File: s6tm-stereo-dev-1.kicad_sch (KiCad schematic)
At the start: 40 parts, among them J10 Conn_01x04_Pin, J3 USB_C_Receptacle_USB2.0_14P, SW1 SW_SPDT, SW10 SW_Push, SW5 SW_Push, SW6 SW_Push, SW7 SW_Push, SW9 SW_Push, U4 ESP32-S3FN8, Y1 48M

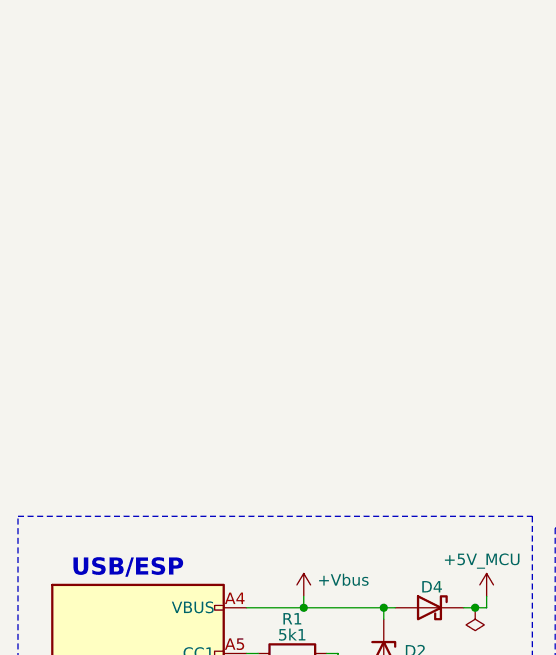
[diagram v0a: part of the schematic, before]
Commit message: schem: add led pwr status
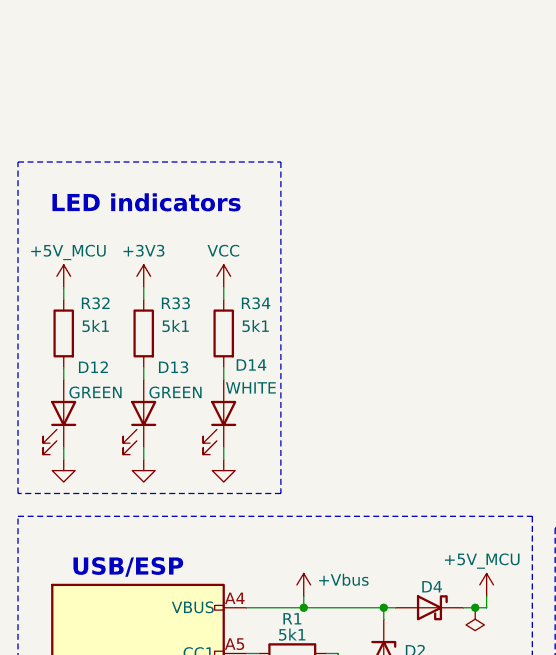
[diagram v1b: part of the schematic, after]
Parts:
- added D12, D13: GREEN, LED_SMD:LED_0805_2012Metric, symbol Device:LED
- added D14: WHITE, LED_SMD:LED_0603_1608Metric, symbol Device:LED
- added R32, R33, R34: 5k1, Resistor_SMD:R_0402_1005Metric, symbol Device:R
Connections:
- net +3V3: now also R33.1
- net +5V_MCU: now also R32.1
- net GND: now also D12.1 (K), D13.1 (K), D14.1 (K)
- new net: D12.2 (A), R32.2
- new net: D14.2 (A), R34.2
- new net: D13.2 (A), R33.2
- new net VCC: R34.1
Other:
- note added: "LED indicators"

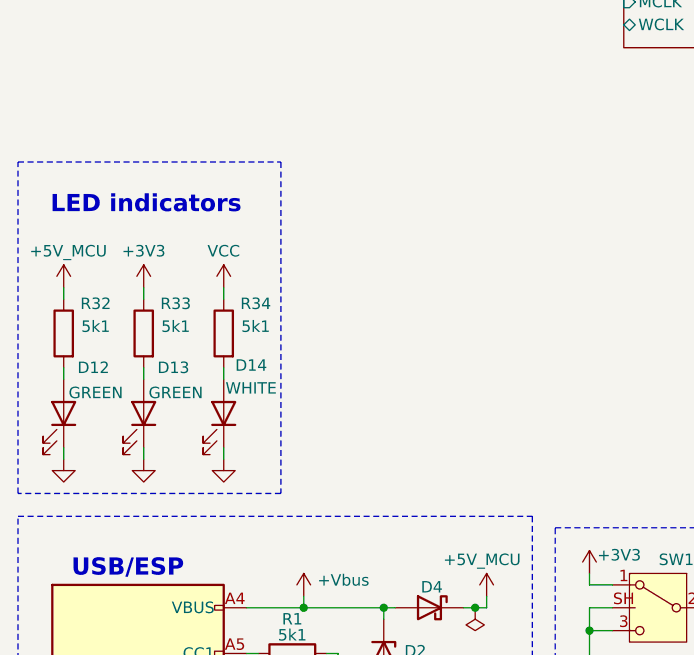
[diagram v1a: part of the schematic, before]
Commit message: schem: add power led indicators for all voltage rails
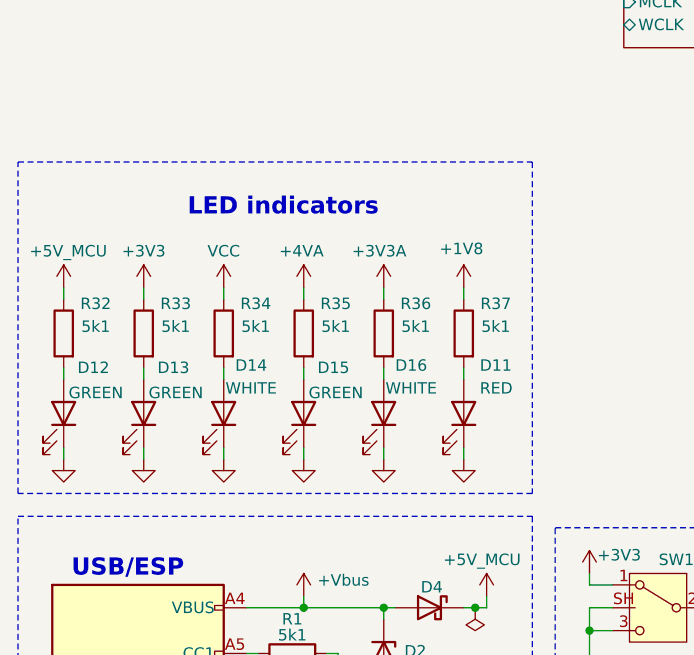
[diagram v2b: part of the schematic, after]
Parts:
- added D11: RED, LED_SMD:LED_0805_2012Metric, symbol Device:LED
- added D15: GREEN, LED_SMD:LED_0805_2012Metric, symbol Device:LED
- added D16: WHITE, LED_SMD:LED_0603_1608Metric, symbol Device:LED
- added R35, R36, R37: 5k1, Resistor_SMD:R_0402_1005Metric, symbol Device:R
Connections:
- net GND: now also D11.1 (K), D15.1 (K), D16.1 (K)
- new net: D15.2 (A), R35.2
- new net: D16.2 (A), R36.2
- new net: D11.2 (A), R37.2
- new net +1V8: R37.1
- new net +3V3A: R36.1
- new net +4VA: R35.1

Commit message: schem: add PG gpio to buck converter
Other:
- sheet Power ports: added PG; removed none
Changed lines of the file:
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@@
+			)
+		)
+		(pin "PG" input
+			(at 107.95 96.52 180)
+			(effects
+				(font
+					(size 1.27 1.27)
+				)
+				(justify left)
 			)
 		)

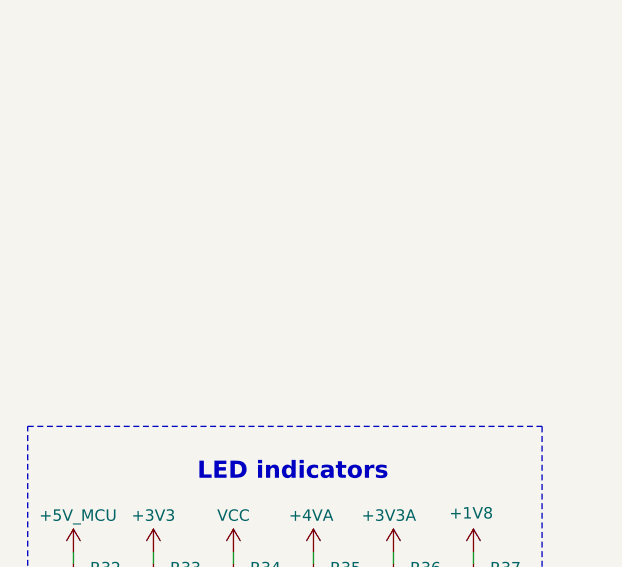
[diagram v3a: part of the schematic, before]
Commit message: schem: add OLED display
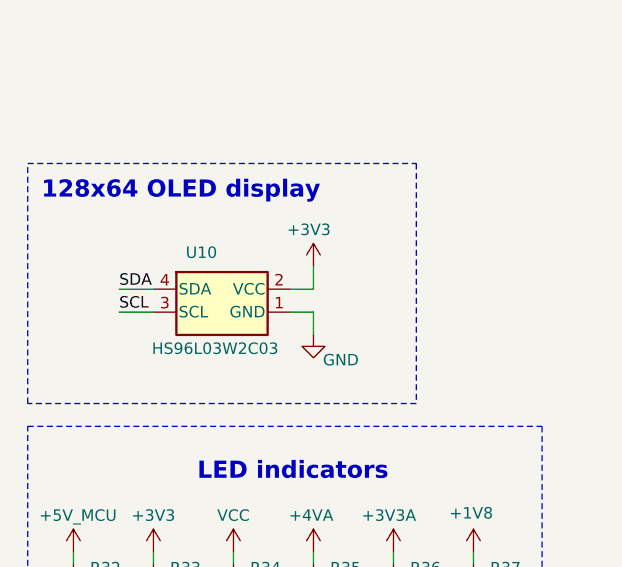
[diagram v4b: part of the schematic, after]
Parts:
- added U10: HS96L03W2C03, Pers:HS96L03W2C03, symbol Pers:HS96L03W2C03
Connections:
- net +3V3: now also U10.2 (VCC)
- net GND: now also U10.1 (GND)
- new net SCL: U10.3 (SCL)
- new net SDA: U10.4 (SDA)
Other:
- note added: "128x64 OLED display"

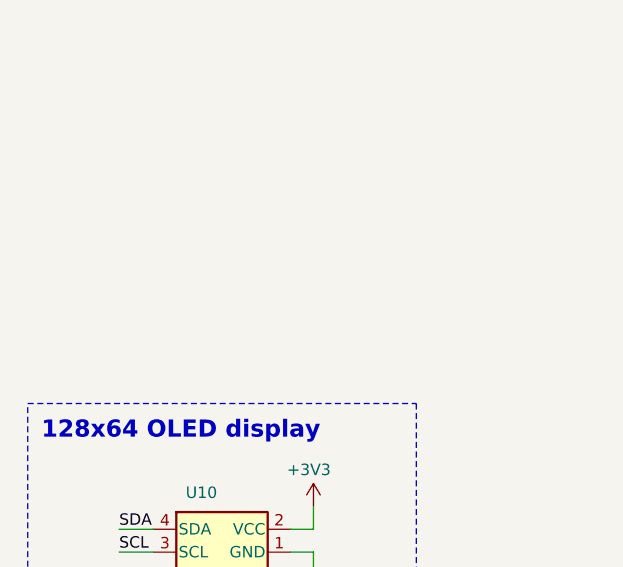
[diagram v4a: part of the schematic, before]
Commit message: schem: add rotary encoder
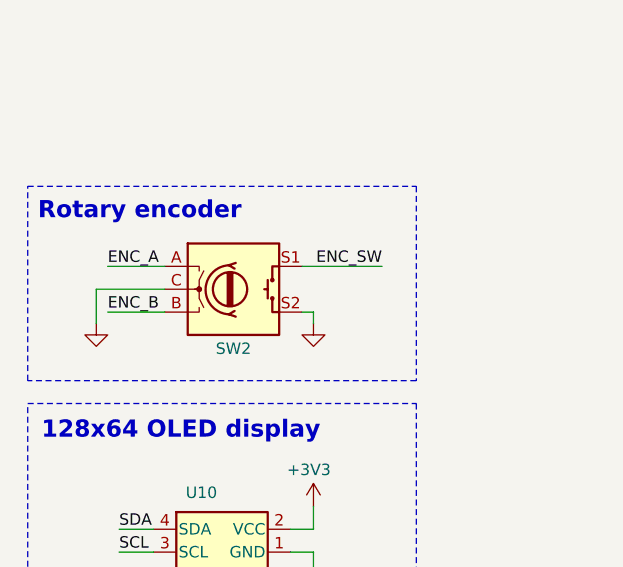
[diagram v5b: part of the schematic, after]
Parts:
- added SW2: RotaryEncoder_Switch, RotaryEncoder_Alps_EC11E-Switch_Vertical_H20mm, symbol Device:RotaryEncoder_Switch
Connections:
- net GND: now also SW2.C, SW2.S2
- new net ENC_A: SW2.A
- new net ENC_B: SW2.B
- new net ENC_SW: SW2.S1
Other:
- note added: "Rotary encoder"

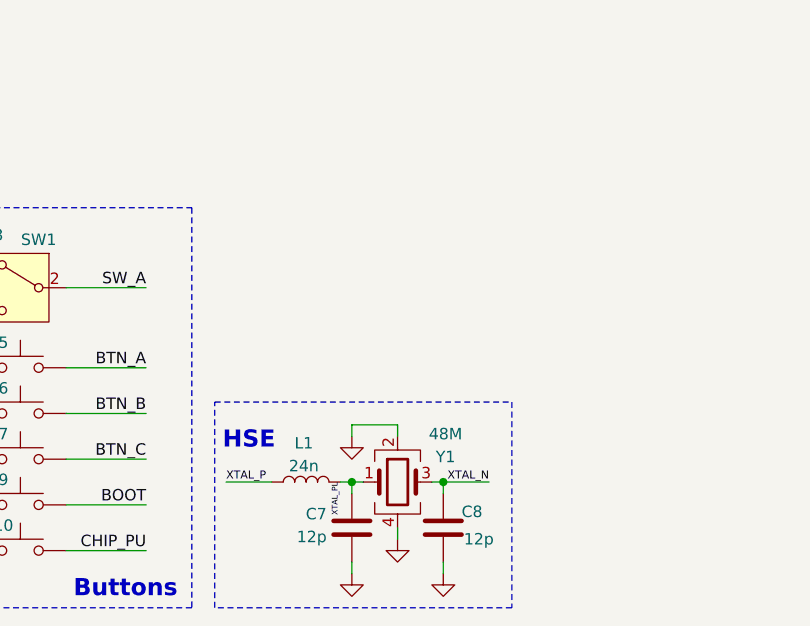
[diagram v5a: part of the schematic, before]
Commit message: schem: add vcc vsense
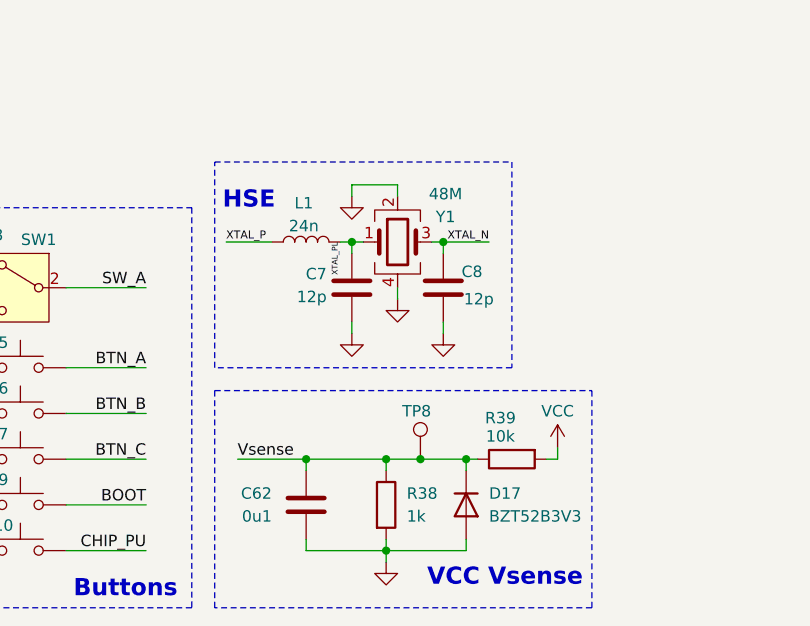
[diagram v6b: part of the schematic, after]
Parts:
- added C62: 0u1, Capacitor_SMD:C_0402_1005Metric, symbol Device:C
- added D17: BZT52B3V3, Diode_SMD:D_SOD-123, symbol Device:D
- added R38: 1k, Resistor_SMD:R_0402_1005Metric, symbol Device:R
- added R39: 10k, Resistor_SMD:R_0402_1005Metric, symbol Device:R
- added TP8: TestPoint, TestPoint:TestPoint_Pad_D2.0mm, symbol Connector:TestPoint
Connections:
- net GND: now also C62.2, D17.2 (A), R38.2
- net VCC: now also R39.2
- new net Vsense: C62.1, D17.1 (K), R38.1, R39.1, TP8.1
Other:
- note added: "VCC Vsense"
- moved on the sheet: C7, C8, L1, Y1

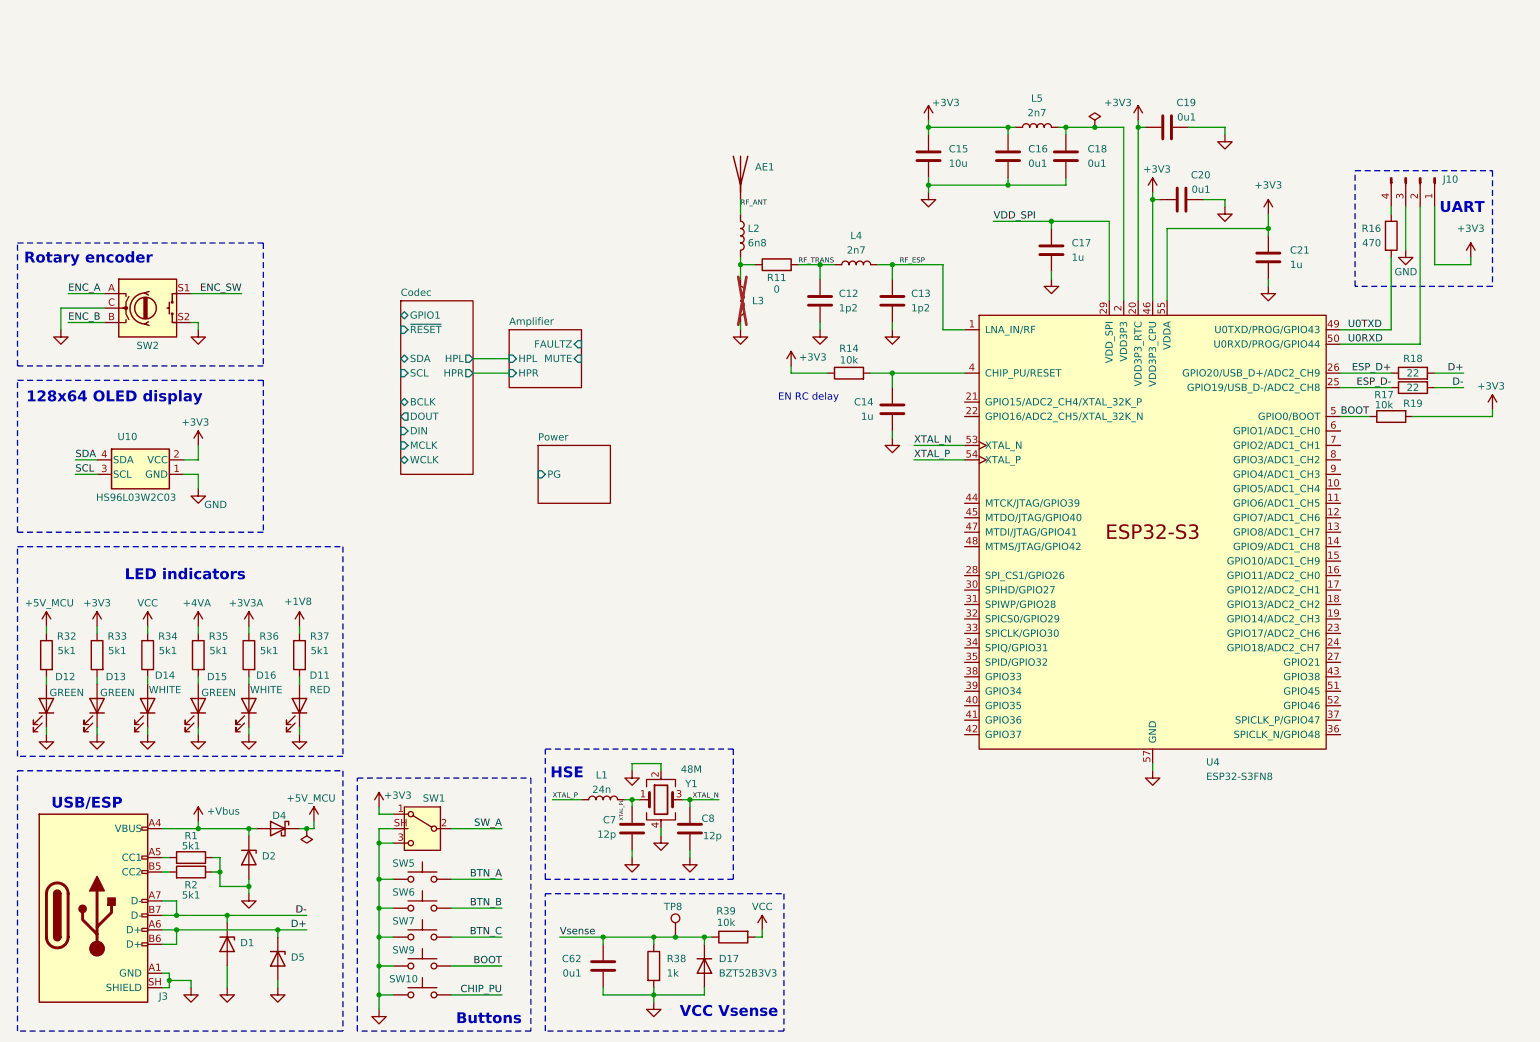
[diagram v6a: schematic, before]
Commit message: schem: connect pheripherals to mcu gpios
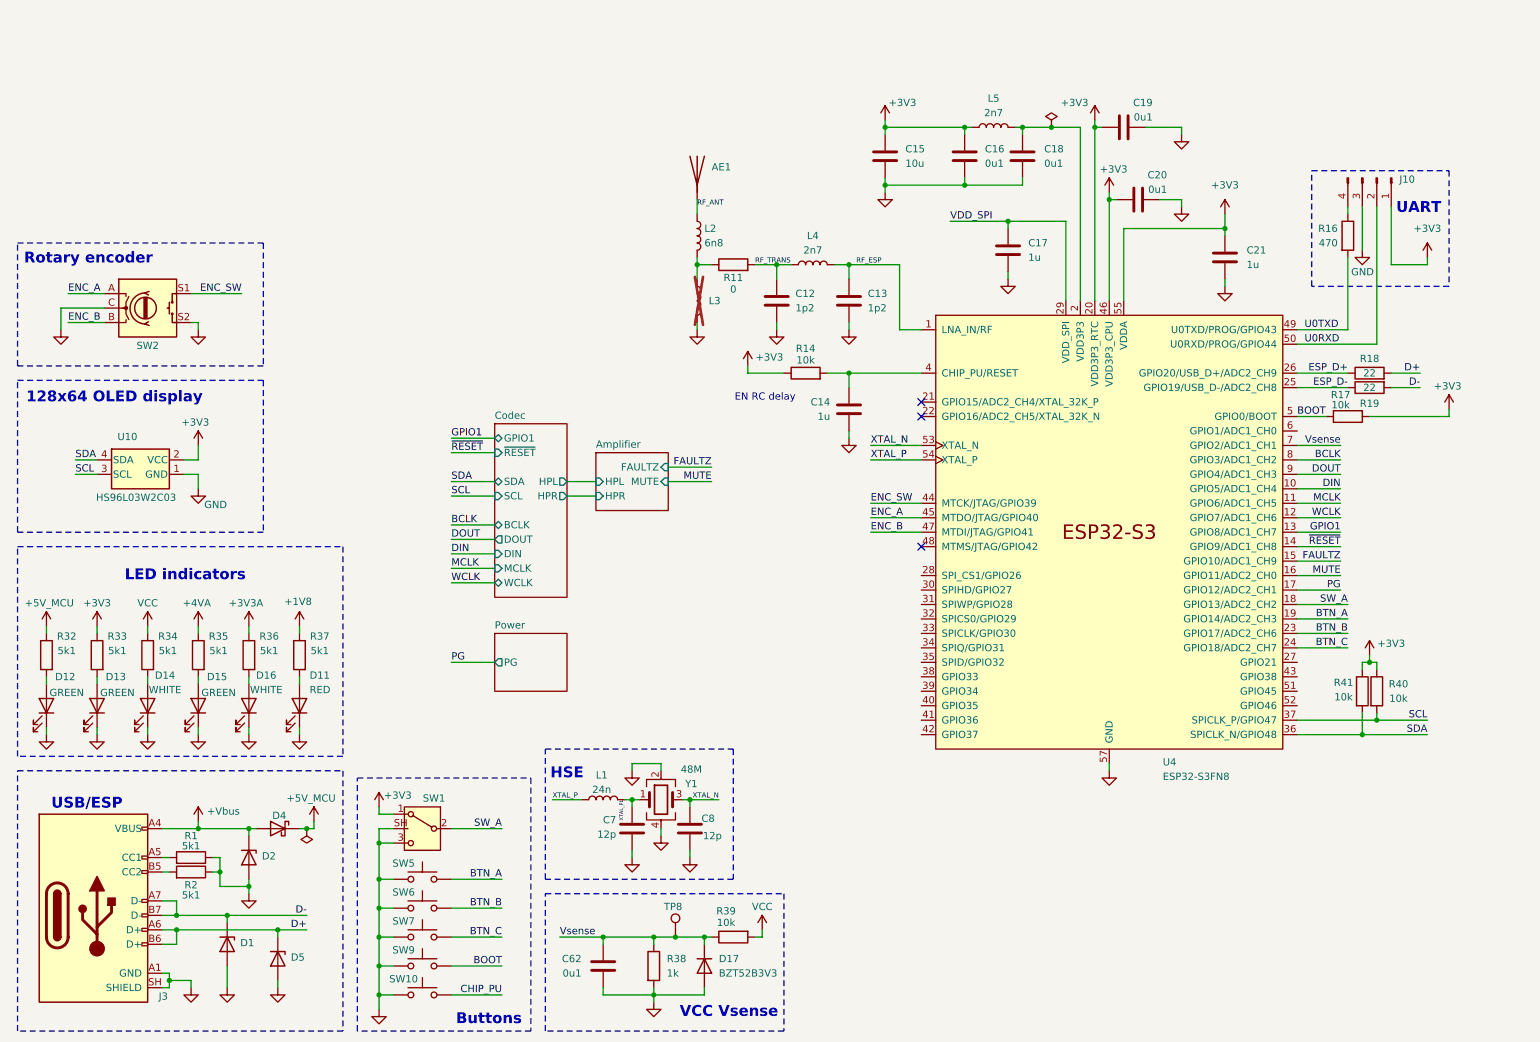
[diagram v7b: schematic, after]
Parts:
- added R40, R41: 10k, Resistor_SMD:R_0402_1005Metric, symbol Device:R
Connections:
- net +3V3: now also R40.1, R41.1
- net BTN_A: now also U4.19 (GPIO14/ADC2_CH3)
- net BTN_B: now also U4.23 (GPIO17/ADC2_CH6)
- net BTN_C: now also U4.24 (GPIO18/ADC2_CH7)
- net ENC_A: now also U4.45 (MTDO/JTAG/GPIO40)
- net ENC_B: now also U4.47 (MTDI/JTAG/GPIO41)
- net ENC_SW: now also U4.44 (MTCK/JTAG/GPIO39)
- net SCL: now also U4.37 (SPICLK_P/GPIO47), R40.2
- net SDA: now also U4.36 (SPICLK_N/GPIO48), R41.2
- net SW_A: now also U4.18 (GPIO13/ADC2_CH2)
- net Vsense: now also U4.7 (GPIO2/ADC1_CH1)
- net DIN: now reaches U4.10 (GPIO5/ADC1_CH4)
- net MCLK: now reaches U4.11 (GPIO6/ADC1_CH5)
- net WCLK: now reaches U4.12 (GPIO7/ADC1_CH6)
- net GPIO1: now reaches U4.13 (GPIO8/ADC1_CH7)
- net ~{RESET}: now reaches U4.14 (GPIO9/ADC1_CH8)
- net FAULTZ: now reaches U4.15 (GPIO10/ADC1_CH9)
- net MUTE: now reaches U4.16 (GPIO11/ADC2_CH0)
- net PG: now reaches U4.17 (GPIO12/ADC2_CH1)
- net BCLK: now reaches U4.8 (GPIO3/ADC1_CH2)
- net DOUT: now reaches U4.9 (GPIO4/ADC1_CH3)
- no-connect marks 0 -> 3
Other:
- moved on the sheet: AE1, C12, C13, C14, C15, C16, C17, C18, C19, C20, C21, J10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
